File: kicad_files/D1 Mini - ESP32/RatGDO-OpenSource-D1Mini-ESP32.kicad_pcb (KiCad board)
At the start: 2 copper layers, 55 x 70 mm, 12 parts, among them J1 Screw_Terminal_01x03, J2 Screw_Terminal_01x03, Q1 2N7002, Q2 AO3400A, U2 mini_esp32

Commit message: Fixed Bad PCB Labeling
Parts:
- added J3: Screw_Terminal_01x03, Connector_PinHeader_2.54mm:PinHeader_1x03_P2.54mm_Vertical, F.Cu at (147.3, 111.8)
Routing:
- net Net-(J1-Pin_1): track 59.8 -> 80.2 mm
- net Net-(J1-Pin_2): track 67.0 -> 64.8 mm
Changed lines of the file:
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@@
+    )
+  )
+  (footprint "Connector_PinHeader_2.54mm:PinHeader_1x03_P2.54mm_Vertical" (layer "F.Cu")
+    (at 147.32 111.76 90)
+    (descr "Through hole straight pin header, 1x03, 2.54mm pitch, single row")
+    (tags "Through hole pin header THT 1x03 2.54mm single row")
+    (property "Sheetfile" "RatGDO-OpenSource-D1Mini-ESP32.kicad_sch")
+    (property "Sheetname" "")
+    (property "ki_description" "Generic screw terminal, single row, 01x03, script generated (kicad-library-utils/schlib/autogen/connector/)")
+    (property "ki_keywords" "screw terminal")
+    (attr through_hole)
+    (fp_text reference "J3" (at 0 8.89) (layer "F.SilkS")
+        (effects (font (size 1 1) (thickness 0.15)))
+    )
+    (fp_text value "Screw_Terminal_01x03" (at 0 7.41 90) (layer "F.Fab")
+        (effects (font (size 1 1) (thickness 0.15)))
+    )
+    (fp_text user "${REFERENCE}" (at 0 2.54) (layer "F.Fab")
+        (effects (font (size 1 1) (thickness 0.15)))
+    )
+    (fp_line (start -1.33 -1.33) (end 0 -1.33)
+      (stroke (width 0.12) (type solid)) (layer "F.SilkS"))
+    (fp_line (start -1.33 0) (end -1.33 -1.33)
+      (stroke (width 0.12) (type solid)) (layer "F.SilkS"))
+    (fp_line (start -1.33 1.27) (end -1.33 6.41)
+      (stroke (width 0.12) (type solid)) (layer "F.SilkS"))
+    (fp_line (start -1.33 1.27) (end 1.33 1.27)
+      (stroke (width 0.12) (type solid)) (layer "F.SilkS"))
+    (fp_line (start -1.33 6.41) (end 1.33 6.41)
+      (stroke (width 0.12) (type solid)) (layer "F.SilkS"))
+    (fp_line (start 1.33 1.27) (end 1.33 6.41)
+      (stroke (width 0.12) (type solid)) (layer "F.SilkS"))
+    (fp_line (start -1.8 -1.8) (end -1.8 6.85)
+      (stroke (width 0.05) (type solid)) (layer "F.CrtYd"))
+    (fp_line (start -1.8 6.85) (end 1.8 6.85)
+      (stroke (width 0.05) (type solid)) (layer "F.CrtYd"))
+    (fp_line (start 1.8 -1.8) (end -1.8 -1.8)
+      (stroke (width 0.05) (type solid)) (layer "F.CrtYd"))
+    (fp_line (start 1.8 6.85) (end 1.8 -1.8)
+      (stroke (width 0.05) (type solid)) (layer "F.CrtYd"))
+    (fp_line (start -1.27 -0.635) (end -0.635 -1.27)
+      (stroke (width 0.1) (type solid)) (layer "F.Fab"))
+    (fp_line (start -1.27 6.35) (end -1.27 -0.635)
+      (stroke (width 0.1) (type solid)) (layer "F.Fab"))
+    (fp_line (start -0.635 -1.27) (end 1.27 -1.27)
+      (stroke (width 0.1) (type solid)) (layer "F.Fab"))
+    (fp_line (start 1.27 -1.27) (end 1.27 6.35)
+      (stroke (width 0.1) (type solid)) (layer "F.Fab"))
+    (fp_line (start 1.27 6.35) (end -1.27 6.35)
+      (stroke (width 0.1) (type solid)) (layer "F.Fab"))
+    (pad "1" thru_hole rect (at 0 0 90) (size 1.7 1.7) (drill 1) (layers "*.Cu" "*.Mask")
+      (net 2 "Net-(J1-Pin_1)") (pinfunction "Pin_1") (pintype "passive"))
+    (pad "2" thru_hole oval (at 0 2.54 90) (size 1.7 1.7) (drill 1) (layers "*.Cu" "*.Mask")
+      (net 1 "Net-(J1-Pin_2)") (pinfunction "Pin_2") (pintype "passive"))
+    (pad "3" thru_hole oval (at 0 5.08 90) (size 1.7 1.7) (drill 1) (layers "*.Cu" "*.Mask")
+      (net 6 "GND") (pinfunction "Pin_3") (pintype "passive"))
+    (model "${KICAD6_3DMODEL_DIR}/Connector_PinHeader_2.54mm.3dshapes/PinHeader_1x03_P2.54mm_Vertical.wrl"
+      (offset (xyz 0 0 0))
+      (scale (xyz 1 1 1))
+      (rotate (xyz 0 0 0))
     )
   )
@@
     (descr "Generic Phoenix Contact connector footprint for: MCV_1,5/3-G-3.5; number of pins: 03; pin pitch: 3.50mm; Vertical || order number: 1843619 8A 160V")
     (tags "phoenix_contact connector MCV_01x03_G_3.5mm")
-    (property "Sheetfile" "RatGDO-OpenSource.kicad_sch")
+    (property "Sheetfile" "RatGDO-OpenSource-D1Mini-ESP32.kicad_sch")
     (property "Sheetname" "")
     (property "ki_description" "Generic screw terminal, single row, 01x03, script generated (kicad-library-utils/schlib/autogen/connector/)")
@@
     (effects (font (size 1 1) (thickness 0.15)) (justify bottom))
   )
-  (gr_text "Only 1 Terminal Block Needs Populated.\nThe Choice Is Yours." (at 140.97 111.76) (layer "F.SilkS")
-    (effects (font (size 1 1) (thickness 0.15)) (justify bottom))
+  (gr_text "Only 1 Terminal Block Needs Populated.\nThe Choice Is Yours." (at 125.437869 111.57816) (layer "F.SilkS")
+    (effects (font (size 1 1) (thickness 0.15)) (justify left bottom))
   )
   (gr_text "BLK\nOBST" (at 139.626103 126.499836) (layer "F.SilkS")
@@
   (segment (start 160.75 83.375) (end 159.6875 84.4375) (width 0.25) (layer "F.Cu") (net 1))
   (segment (start 160.75 76.93) (end 160.75 83.375) (width 0.25) (layer "F.Cu") (net 1))
-  (segment (start 148.59 114.3) (end 152.4 114.3) (width 0.25) (layer "F.Cu") (net 1))
+  (segment (start 159.6875 84.4375) (end 159.6875 100.33) (width 0.25) (layer "F.Cu") (net 1))
+  (segment (start 149.86 111.76) (end 148.59 113.03) (width 0.25) (layer "F.Cu") (net 1))
   (segment (start 160.02 76.2) (end 160.75 76.93) (width 0.25) (layer "F.Cu") (net 1))
   (segment (start 148.59 114.3) (end 150.17 115.88) (width 0.25) (layer "F.Cu") (net 1))
+  (segment (start 148.59 113.03) (end 148.59 114.3) (width 0.25) (layer "F.Cu") (net 1))
   (segment (start 138.815 114.3) (end 148.59 114.3) (width 0.25) (layer "F.Cu") (net 1))
   (segment (start 134.7 118.415) (end 138.815 114.3) (width 0.25) (layer "F.Cu") (net 1))
-  (segment (start 159.6875 84.4375) (end 159.6875 107.0125) (width 0.25) (layer "F.Cu") (net 1))
+  (segment (start 149.86 111.76) (end 159.6875 101.9325) (width 0.25) (layer "F.Cu") (net 1))
   (segment (start 150.17 115.88) (end 150.17 119.38) (width 0.25) (layer "F.Cu") (net 1))
-  (segment (start 159.6875 107.0125) (end 152.4 114.3) (width 0.25) (layer "F.Cu") (net 1))
+  (segment (start 159.6875 101.9325) (end 159.6875 100.33) (width 0.25) (layer "F.Cu") (net 1))
   (segment (start 129.7 118.415) (end 122.2775 110.9925) (width 0.25) (layer "F.Cu") (net 2))
   (segment (start 129.7 118.415) (end 129.7 120.81) (width 0.25) (layer "F.Cu") (net 2))
   (segment (start 144.13 121.92) (end 146.67 119.38) (width 0.25) (layer "F.Cu") (net 2))
   (segment (start 122.2775 110.9925) (end 122.2775 82.55) (width 0.25) (layer "F.Cu") (net 2))
+  (segment (start 129.7 118.415) (end 136.355 111.76) (width 0.25) (layer "F.Cu") (net 2))
   (segment (start 129.7 120.81) (end 130.81 121.92) (width 0.25) (layer "F.Cu") (net 2))
+  (segment (start 136.355 111.76) (end 147.32 111.76) (width 0.25) (layer "F.Cu") (net 2))
   (segment (start 130.81 121.92) (end 144.13 121.92) (width 0.25) (layer "F.Cu") (net 2))
   (segment (start 157.8125 83.4875) (end 155.965 81.64) (width 0.25) (layer "F.Cu") (net 3))

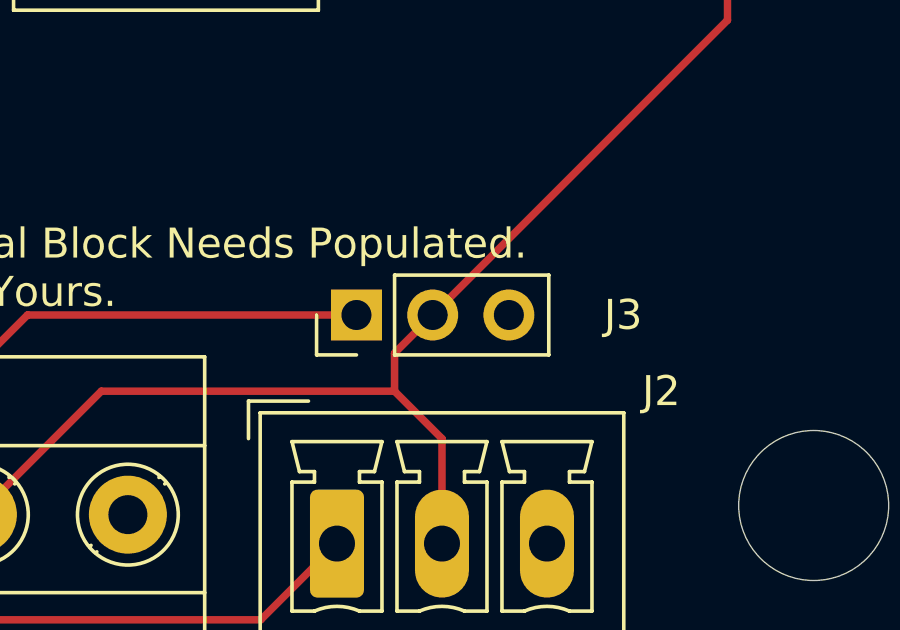
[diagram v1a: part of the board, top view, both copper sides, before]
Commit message: Change Pin Header to Pin Socket
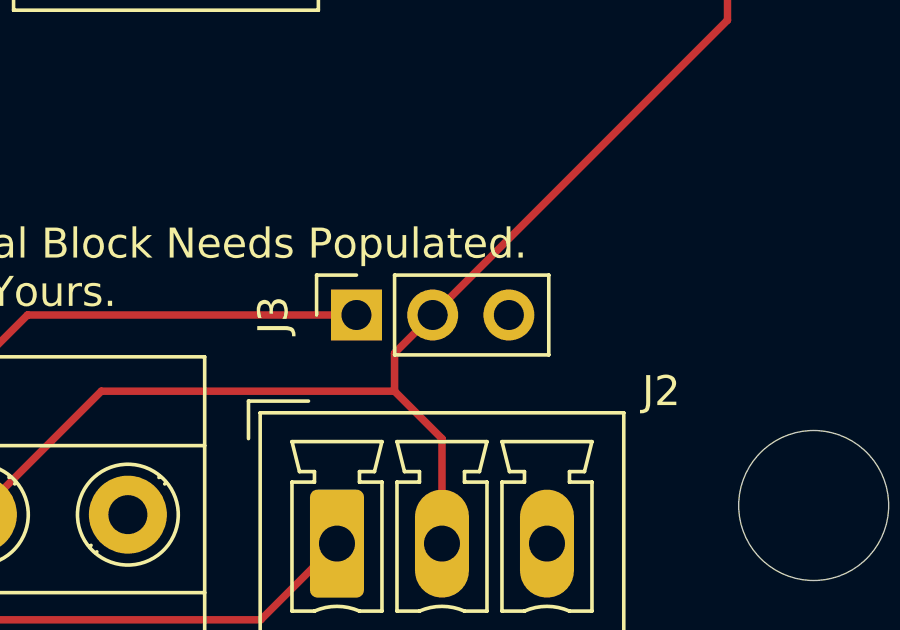
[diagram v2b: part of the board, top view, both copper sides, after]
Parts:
- J3: footprint Connector_PinHeader_2.54mm:PinHeader_1x03_P2.54mm_Vertical -> Connector_PinSocket_2.54mm:PinSocket_1x03_P2.54mm_Vertical
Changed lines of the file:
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@@
     )
   )
-  (footprint "Connector_PinHeader_2.54mm:PinHeader_1x03_P2.54mm_Vertical" (layer "F.Cu")
+  (footprint "Connector_PinSocket_2.54mm:PinSocket_1x03_P2.54mm_Vertical" (layer "F.Cu")
     (at 147.32 111.76 90)
-    (descr "Through hole straight pin header, 1x03, 2.54mm pitch, single row")
-    (tags "Through hole pin header THT 1x03 2.54mm single row")
+    (descr "Through hole straight socket strip, 1x03, 2.54mm pitch, single row (from Kicad 4.0.7), script generated")
+    (tags "Through hole socket strip THT 1x03 2.54mm single row")
     (property "Sheetfile" "RatGDO-OpenSource-D1Mini-ESP32.kicad_sch")
     (property "Sheetname" "")
@@
     (property "ki_keywords" "screw terminal")
     (attr through_hole)
-    (fp_text reference "J3" (at 0 8.89) (layer "F.SilkS")
+    (fp_text reference "J3" (at 0 -2.77 90) (layer "F.SilkS")
         (effects (font (size 1 1) (thickness 0.15)))
     )
-    (fp_text value "Screw_Terminal_01x03" (at 0 7.41 90) (layer "F.Fab")
+    (fp_text value "Screw_Terminal_01x03" (at 0 7.85 90) (layer "F.Fab")
         (effects (font (size 1 1) (thickness 0.15)))
     )
-    (fp_text user "${REFERENCE}" (at 0 2.54) (layer "F.Fab")
+    (fp_text user "${REFERENCE}" (at 0 2.54 180) (layer "F.Fab")
         (effects (font (size 1 1) (thickness 0.15)))
     )
-    (fp_line (start -1.33 -1.33) (end 0 -1.33)
-      (stroke (width 0.12) (type solid)) (layer "F.SilkS"))
-    (fp_line (start -1.33 0) (end -1.33 -1.33)
-      (stroke (width 0.12) (type solid)) (layer "F.SilkS"))
     (fp_line (start -1.33 1.27) (end -1.33 6.41)
       (stroke (width 0.12) (type solid)) (layer "F.SilkS"))
@@
     (fp_line (start -1.33 6.41) (end 1.33 6.41)
       (stroke (width 0.12) (type solid)) (layer "F.SilkS"))
+    (fp_line (start 0 -1.33) (end 1.33 -1.33)
+      (stroke (width 0.12) (type solid)) (layer "F.SilkS"))
+    (fp_line (start 1.33 -1.33) (end 1.33 0)
+      (stroke (width 0.12) (type solid)) (layer "F.SilkS"))
     (fp_line (start 1.33 1.27) (end 1.33 6.41)
       (stroke (width 0.12) (type solid)) (layer "F.SilkS"))
-    (fp_line (start -1.8 -1.8) (end -1.8 6.85)
+    (fp_line (start -1.8 -1.8) (end 1.75 -1.8)
       (stroke (width 0.05) (type solid)) (layer "F.CrtYd"))
-    (fp_line (start -1.8 6.85) (end 1.8 6.85)
+    (fp_line (start -1.8 6.85) (end -1.8 -1.8)
       (stroke (width 0.05) (type solid)) (layer "F.CrtYd"))
-    (fp_line (start 1.8 -1.8) (end -1.8 -1.8)
+    (fp_line (start 1.75 -1.8) (end 1.75 6.85)
       (stroke (width 0.05) (type solid)) (layer "F.CrtYd"))
-    (fp_line (start 1.8 6.85) (end 1.8 -1.8)
+    (fp_line (start 1.75 6.85) (end -1.8 6.85)
       (stroke (width 0.05) (type solid)) (layer "F.CrtYd"))
-    (fp_line (start -1.27 -0.635) (end -0.635 -1.27)
+    (fp_line (start -1.27 -1.27) (end 0.635 -1.27)
       (stroke (width 0.1) (type solid)) (layer "F.Fab"))
-    (fp_line (start -1.27 6.35) (end -1.27 -0.635)
+    (fp_line (start -1.27 6.35) (end -1.27 -1.27)
       (stroke (width 0.1) (type solid)) (layer "F.Fab"))
-    (fp_line (start -0.635 -1.27) (end 1.27 -1.27)
+    (fp_line (start 0.635 -1.27) (end 1.27 -0.635)
       (stroke (width 0.1) (type solid)) (layer "F.Fab"))
-    (fp_line (start 1.27 -1.27) (end 1.27 6.35)
+    (fp_line (start 1.27 -0.635) (end 1.27 6.35)
       (stroke (width 0.1) (type solid)) (layer "F.Fab"))
     (fp_line (start 1.27 6.35) (end -1.27 6.35)
@@
     (pad "3" thru_hole oval (at 0 5.08 90) (size 1.7 1.7) (drill 1) (layers "*.Cu" "*.Mask")
       (net 6 "GND") (pinfunction "Pin_3") (pintype "passive"))
-    (model "${KICAD6_3DMODEL_DIR}/Connector_PinHeader_2.54mm.3dshapes/PinHeader_1x03_P2.54mm_Vertical.wrl"
+    (model "${KICAD6_3DMODEL_DIR}/Connector_PinSocket_2.54mm.3dshapes/PinSocket_1x03_P2.54mm_Vertical.wrl"
       (offset (xyz 0 0 0))
       (scale (xyz 1 1 1))

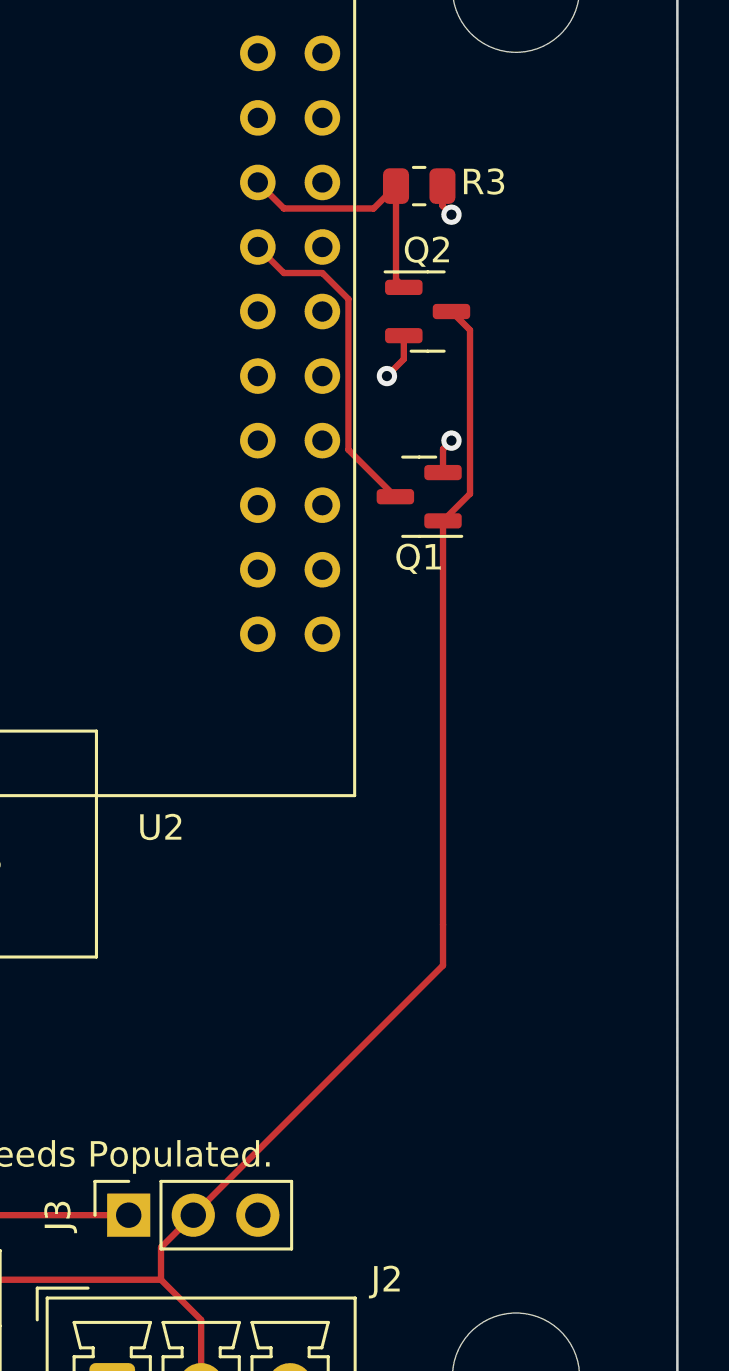
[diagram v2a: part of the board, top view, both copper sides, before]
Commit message: Cleaning up Schematics and making PCB layout similar for D1 Boards
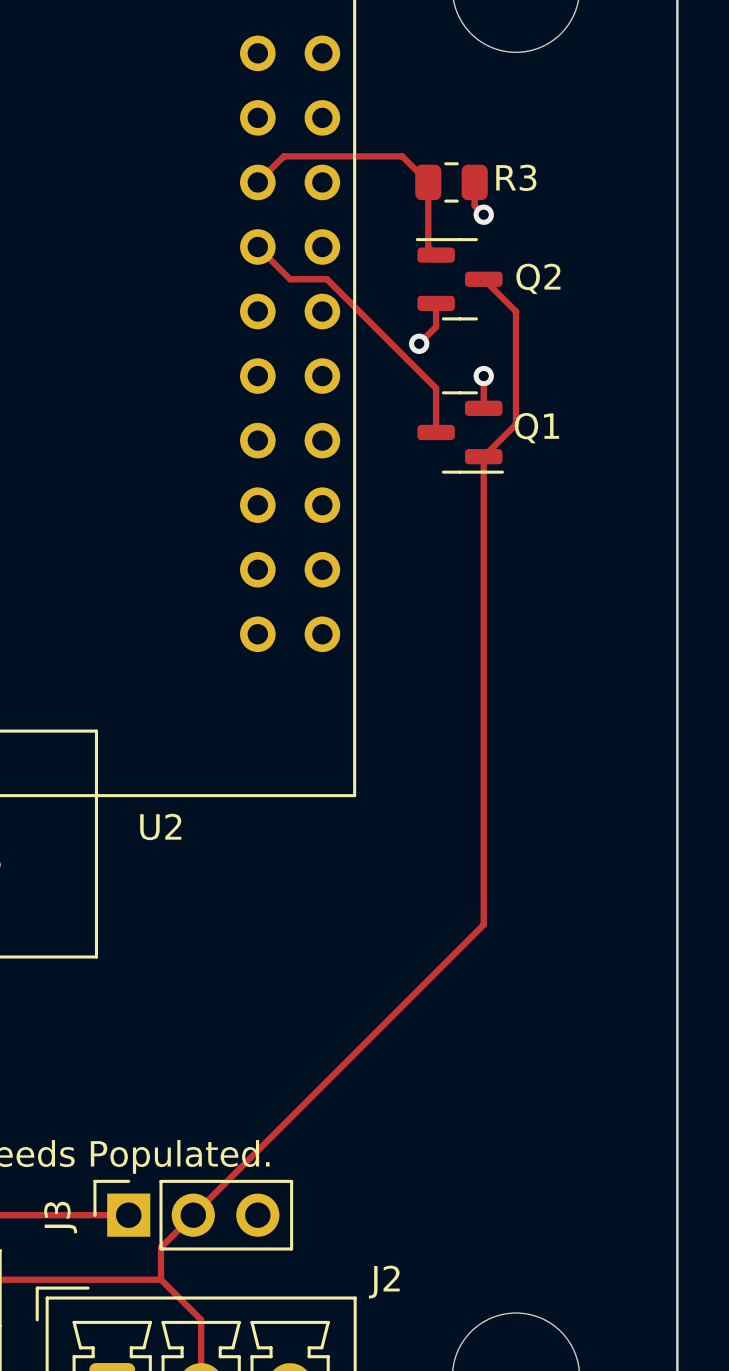
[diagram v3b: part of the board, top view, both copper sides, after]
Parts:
- moved Q1 2.99 mm to (160.4, 81.0)
- moved Q2 1.80 mm to (160.4, 74.9)
- moved R3 1.28 mm to (160.0, 71.1)
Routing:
- net Net-(J1-RED/CTRL): track 64.8 -> 67.0 mm
- net Net-(Q1-D): track 13.0 -> 11.1 mm

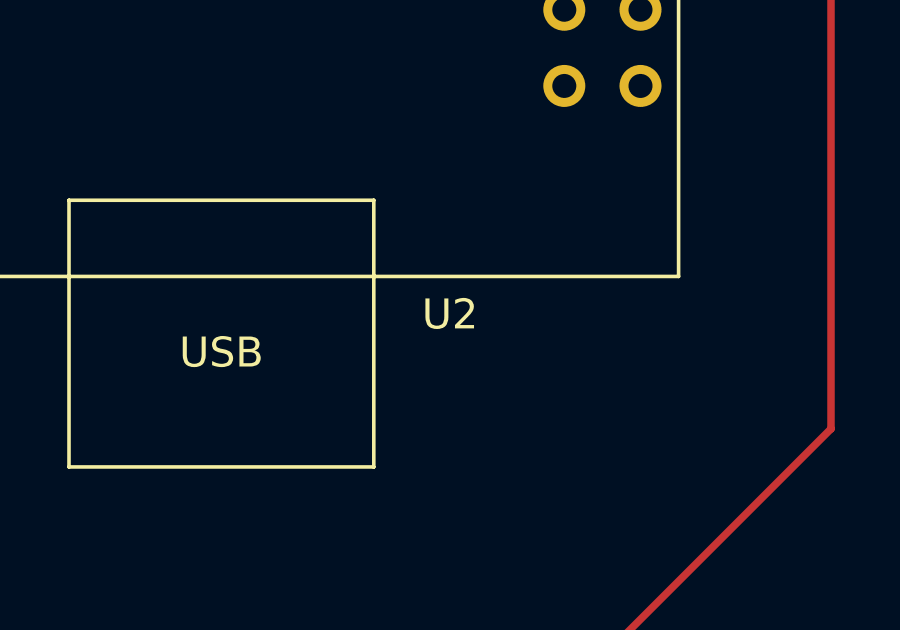
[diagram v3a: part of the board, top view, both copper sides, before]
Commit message: Added Bare ESP8266 kicad files.
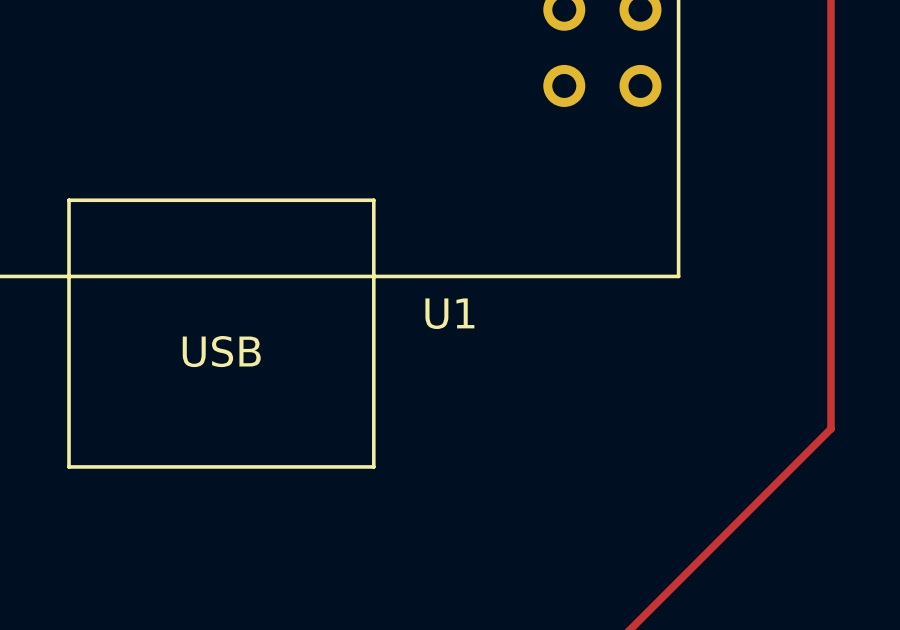
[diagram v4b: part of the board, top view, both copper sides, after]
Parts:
- renumbered U2 to U1
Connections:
- R1 pad 2: Net-(U2-IO_23/D7) -> Net-(U1-IO_23/D7)
- R2 pad 1: Net-(U2-IO_23/D7) -> Net-(U1-IO_23/D7)
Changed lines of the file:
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@@
   (net 41 "unconnected-(U2-GND-Pad1)")
   (net 42 "unconnected-(U2-RST-Pad2)")
+  (net 43 "Net-(U1-IO_23{slash}D7)")
   (footprint "Resistor_SMD:R_0805_2012Metric" (layer "F.Cu")
     (at 160.02 71.12 180)
@@
     (property "Sheetname" "")
     (attr through_hole)
-    (fp_text reference "U2" (at 7.62 19.05) (layer "F.SilkS")
+    (fp_text reference "U1" (at 7.62 19.05) (layer "F.SilkS")
         (effects (font (size 1 1) (thickness 0.15)))
     )
@@
       (stroke (width 0.1) (type solid)) (layer "F.Fab"))
     (pad "1" smd roundrect (at -0.9125 0 180) (size 1.025 1.4) (layers "F.Cu" "F.Paste" "F.Mask") (roundrect_rratio 0.243902439)
-      (net 8 "Net-(U2-IO_23{slash}D7)") (pintype "passive"))
+      (net 43 "Net-(U1-IO_23{slash}D7)") (pintype "passive"))
     (pad "2" smd roundrect (at 0.9125 0 180) (size 1.025 1.4) (layers "F.Cu" "F.Paste" "F.Mask") (roundrect_rratio 0.243902439)
       (net 6 "GND") (pintype "passive"))
@@
       (net 1 "Net-(J1-BLK{slash}OBST)") (pintype "passive"))
     (pad "2" smd roundrect (at 0.9125 0) (size 1.025 1.4) (layers "F.Cu" "F.Paste" "F.Mask") (roundrect_rratio 0.243902439)
-      (net 8 "Net-(U2-IO_23{slash}D7)") (pintype "passive"))
+      (net 43 "Net-(U1-IO_23{slash}D7)") (pintype "passive"))
     (model "${KICAD6_3DMODEL_DIR}/Resistor_SMD.3dshapes/R_0805_2012Metric.wrl"
       (offset (xyz 0 0 0))
